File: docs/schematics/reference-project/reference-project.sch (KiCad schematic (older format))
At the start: 8 parts, among them SW1 RESET, SW2 INPUT_5, U1 ATTINY85-20PU

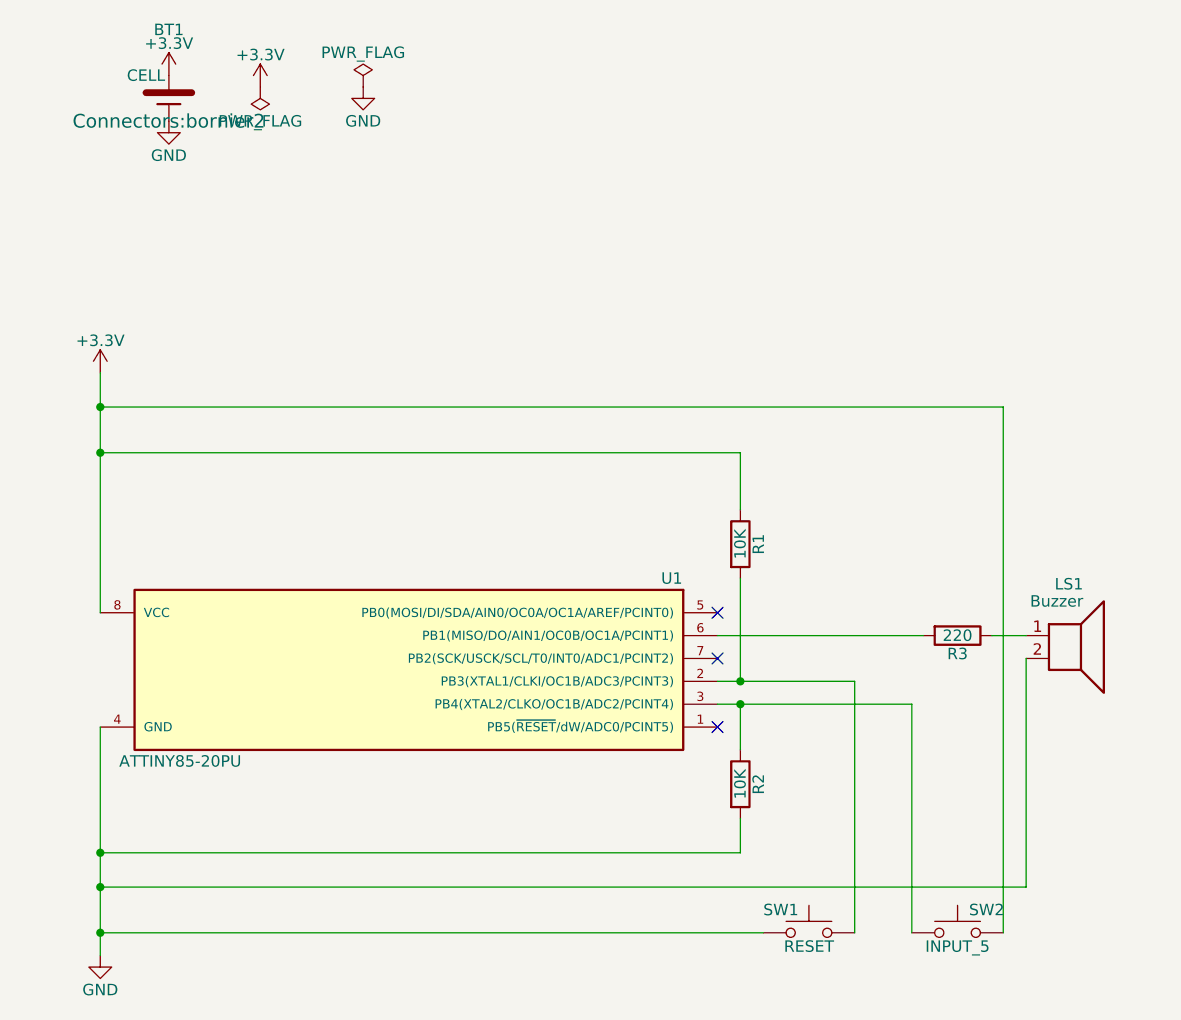
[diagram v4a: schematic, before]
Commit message: Full SMD version.
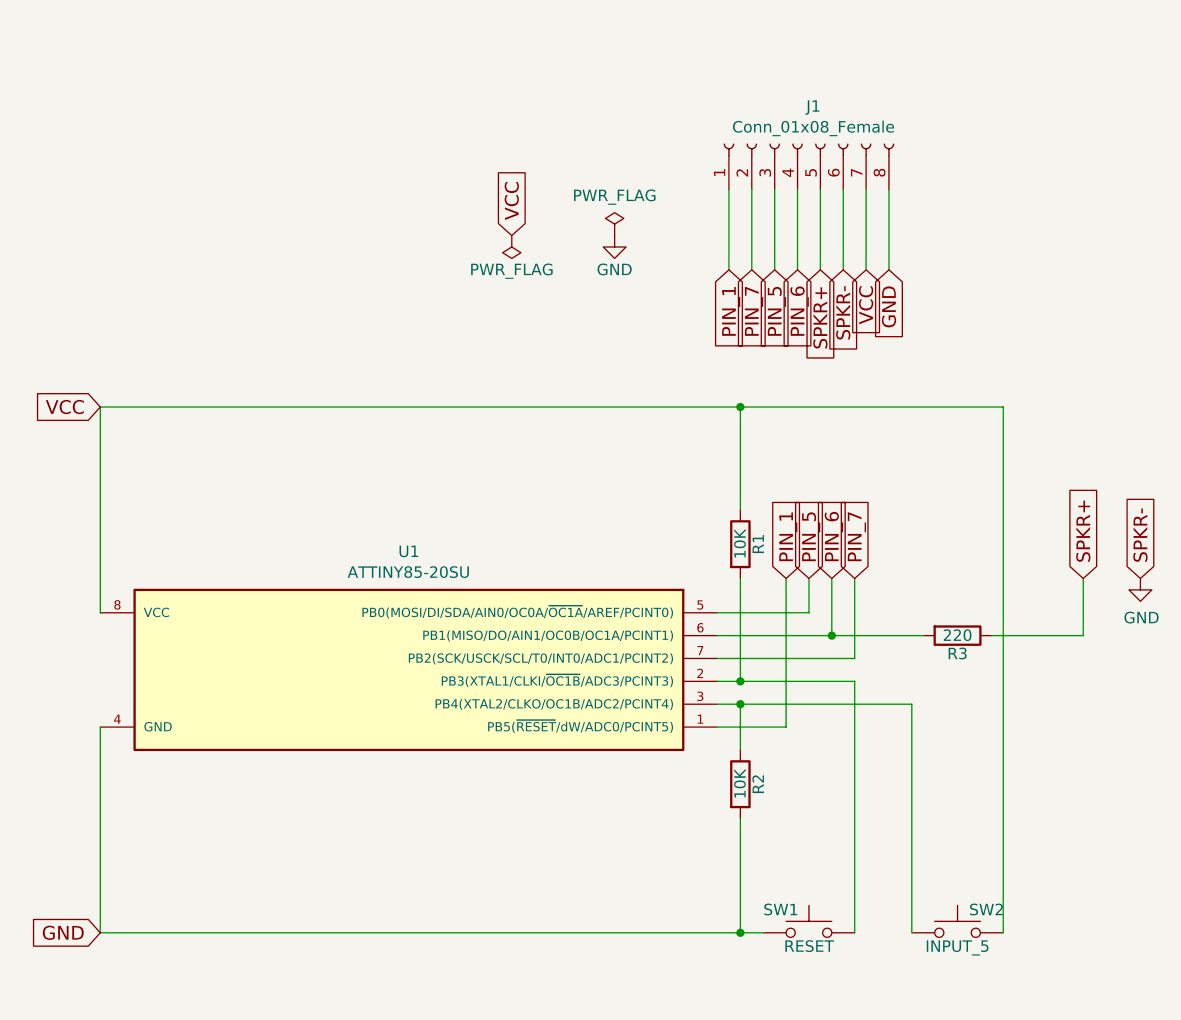
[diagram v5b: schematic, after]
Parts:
- removed BT1: CELL, Connectors:bornier2, symbol CELL
- removed LS1: Buzzer, Buzzers_Beepers:Buzzer_12x9.5RM7.6, symbol Speaker
- removed U1: ATTINY85-20PU, Housings_DIP:DIP-8_W7.62mm, symbol ATTINY85-20PU
- added J1: Conn_01x08_Female, conn-100mil:CONN-100MIL-F-1x8, symbol Conn_01x08_Female
- added U1: ATTINY85-20SU, Housings_SOIC:SOIC-8_3.9x4.9mm_Pitch1.27mm, symbol ATTINY85-20SU
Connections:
- net GND: now also J1.6 (Pin_6), J1.8 (Pin_8), U1.4 (GND)
- net at R1.2, SW1.2: now also U1.2 (PB3(XTAL1/CLKI/~OC1B~/ADC3/PCINT3))
- net at R2.1, SW2.1: now also U1.3 (PB4(XTAL2/CLKO/OC1B/ADC2/PCINT4))
- net PIN_6: now reaches R3.2
- net PIN_6: now also J1.4 (Pin_4), U1.6 (PB1(MISO/DO/AIN1/OC0B/OC1A/PCINT1))
- net SPKR+: now reaches R3.1
- net SPKR+: now also J1.5 (Pin_5)
- net +3V3 renamed VCC
- net VCC: now also J1.7 (Pin_7), U1.8 (VCC)
- new net PIN_1: J1.1 (Pin_1), U1.1 (PB5(~RESET~/dW/ADC0/PCINT5))
- new net PIN_5: J1.3 (Pin_3), U1.5 (PB0(MOSI/DI/SDA/AIN0/OC0A/~OC1A~/AREF/PCINT0))
- new net PIN_7: J1.2 (Pin_2), U1.7 (PB2(SCK/USCK/SCL/T0/INT0/ADC1/PCINT2))
- no-connect marks 3 -> 0
